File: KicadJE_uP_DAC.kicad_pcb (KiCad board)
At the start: 2 copper layers, 100 x 100 mm, 199 parts, among them J201 CV1, J202 CV2, J203 OUT1, J204 OUT2, J205 IN1, J206 IN2, J301 AVR-ISP-6, J302 UART, J401 CV1, J402 CV2, J403 OUT1, J404 OUT2, J405 OUT3, J406 OUT4, J407 IN1, J408 IN2, J409 I2C, J501 BOOT, J502 UART, J503 USB_B_Micro, P201 Doepfer_Power_16pin, P401 Doepfer_Power_16pin, SW201 SW_SPDT, SW401 SW_SPDT, U201 TL072, U202 MCP4822, U301 ATmega32A-AU, U401 TL072, U402 TL072, U405 MCP4822, U501 AMS1117-3.3, U502 STM32F103C8Tx, Y301 16MHz, Y501 8 MHz

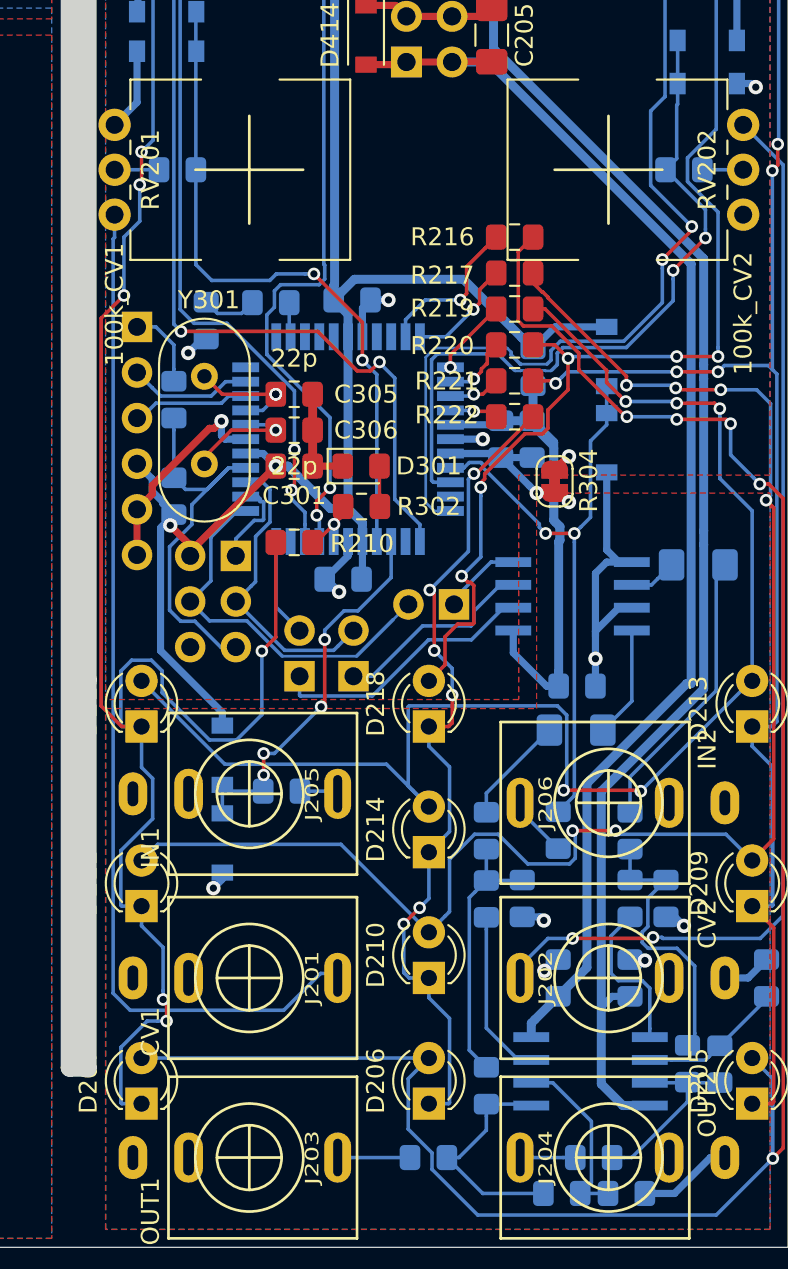
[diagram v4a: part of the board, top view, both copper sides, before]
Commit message: Silk update - DDS1 and DDS2 routed
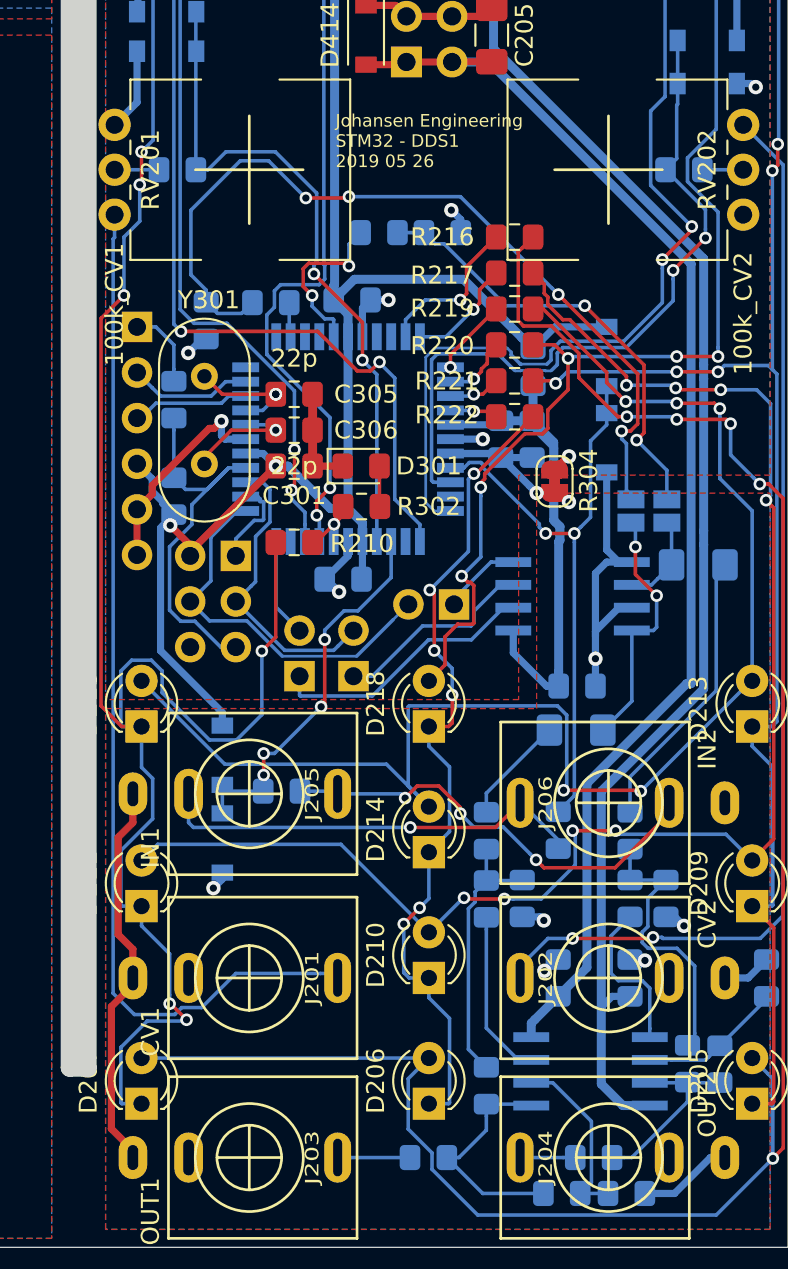
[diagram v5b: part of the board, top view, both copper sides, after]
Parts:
- added C213: 100n, Capacitor_SMD:C_0805_2012Metric_Pad1.15x1.40mm_HandSolder, B.Cu at (130.8, 93.5)
- added JP203: PWM1, Jumper:SolderJumper-2_P1.3mm_Open_Pad1.0x1.5mm, B.Cu at (141.2, 109.0)
- added JP205: PWM2, Jumper:SolderJumper-2_P1.3mm_Open_Pad1.0x1.5mm, B.Cu at (143.2, 109.0)
- added R223: 1k, Resistor_SMD:R_0805_2012Metric_Pad1.15x1.40mm_HandSolder, B.Cu at (127.2, 93.5)
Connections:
- net 0_LED renamed 32_0_LED
- U301 pad 16: (no net) -> 32_15_PWM
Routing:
- net PWM12: track 3.08 -> 47.8 mm, vias 0 -> 4
- net PWM15: track 0.00 -> 25.1 mm, vias 0 -> 2
- net Net-(J205-PadT): track 2.16 -> 24.9 mm, vias 0 -> 3
- net GNDA: track 124.8 -> 146.7 mm
- net Net-(J205-PadTN): track 3.43 -> 24.2 mm, vias 0 -> 1
- net 32_15_PWM: track 0.00 -> 9.63 mm, vias 0 -> 2
- net DACA: track 6.21 -> 14.1 mm, vias 0 -> 2
- net R1_19: track 86.7 -> 84.1 mm, vias 6 -> 8
- net DACB: track 2.67 -> 5.13 mm
- net C2_0: track 119.6 -> 121.2 mm
- net GND: track 179.6 -> 181.0 mm, vias 17 -> 18
- net +5V: track 273.5 -> 274.2 mm
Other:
- board text added: "DDS1"
- board text added: "Johansen Engineering STM32 - DDS1 2019 05 26"
- board text removed: "VCO3"

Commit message: 555 PCB
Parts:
- added C601: 1u, Capacitor_SMD:C_1206_3216Metric_Pad1.42x1.75mm_HandSolder, B.Cu at (70.0, 20.0)
- added C602: 100n, Capacitor_SMD:C_0805_2012Metric_Pad1.15x1.40mm_HandSolder, B.Cu at (62.0, 16.0)
- added C603: 100n, Capacitor_SMD:C_0805_2012Metric_Pad1.15x1.40mm_HandSolder, B.Cu at (79.0, 20.0)
- added C604: 1u, Capacitor_SMD:C_1206_3216Metric_Pad1.42x1.75mm_HandSolder, B.Cu at (70.0, 16.0)
- added C605: 100n, Capacitor_SMD:C_0805_2012Metric_Pad1.15x1.40mm_HandSolder, B.Cu at (87.9, 8.28)
- added C606: 1n, Capacitor_SMD:C_0805_2012Metric_Pad1.15x1.40mm_HandSolder, B.Cu at (84.1, 5.33)
- added C607: 22n, Capacitor_SMD:C_0805_2012Metric_Pad1.15x1.40mm_HandSolder, B.Cu at (80.0, 25.0)
- added C608: 10n, Capacitor_SMD:C_0805_2012Metric_Pad1.15x1.40mm_HandSolder, B.Cu at (75.0, 29.0)
- added C609: 220n, Capacitor_SMD:C_0805_2012Metric_Pad1.15x1.40mm_HandSolder, B.Cu at (102.2, 11.9)
- added C610: 1n, Capacitor_SMD:C_0805_2012Metric_Pad1.15x1.40mm_HandSolder, B.Cu at (83.2, 11.2)
- added C611: 1n, Capacitor_SMD:C_0805_2012Metric_Pad1.15x1.40mm_HandSolder, B.Cu at (89.1, 15.5)
- added D601: 1N1007, Diode_SMD:D_SOD-123, B.Cu at (63.0, 11.0)
- added D602: 1N1007, Diode_SMD:D_SOD-123, B.Cu at (63.0, 20.0)
- added D603: 1N1007, Diode_SMD:D_SOD-123, B.Cu at (120.5, 43.0)
- added D604: 1N1007, Diode_SMD:D_SOD-123, B.Cu at (94.0, 23.0)
- added D605: 1N1007, Diode_SMD:D_SOD-123, B.Cu at (100.9, 20.9)
- added D606: 1N1007, Diode_SMD:D_SOD-123, B.Cu at (94.7, 18.6)
- added D607: LED, LED_THT:LED_D3.0mm, F.Cu at (99.0, 137.0)
- added D609: LED, LED_THT:LED_D3.0mm, F.Cu at (99.0, 149.0)
- added J601: CV1, AJ-Dropbox-Kicad:PJ301SM, F.Cu at (95.0, 130.0)
- added J602: FM_lin, AJ-Dropbox-Kicad:PJ301SM, F.Cu at (95.0, 143.0)
- added J603: Sync, AJ-Dropbox-Kicad:PJ301SM, F.Cu at (95.0, 118.0)
- added J604: PWM, AJ-Dropbox-Kicad:PJ301SM, F.Cu at (95.0, 105.0)
- added J605: Ramp, AJ-Dropbox-Kicad:PJ301SM, F.Cu at (105.0, 118.0)
- added J606: Tri, AJ-Dropbox-Kicad:PJ301SM, F.Cu at (105.0, 144.5)
- added J608: 555_Pulse, AJ-Dropbox-Kicad:PJ301SM, F.Cu at (105.0, 130.0)
- added P601: Doepfer_Power_10pin, Connectors_IDC:IDC-Header_2x05_Pitch2.54mm_Straight, B.Cu at (105.5, 69.5)
- added R601: 10k, Resistor_SMD:R_0805_2012Metric_Pad1.15x1.40mm_HandSolder, B.Cu at (93.9, 15.5)
- added R602: 12k, Resistor_SMD:R_0805_2012Metric_Pad1.15x1.40mm_HandSolder, B.Cu at (85.0, 26.0)
- added R603: 47k, Resistor_SMD:R_0805_2012Metric_Pad1.15x1.40mm_HandSolder, B.Cu at (79.0, 16.0)
- added R604: 150k, Resistor_SMD:R_0805_2012Metric_Pad1.15x1.40mm_HandSolder, B.Cu at (114.1, 34.3)
- added R605: 100k, Resistor_SMD:R_0805_2012Metric_Pad1.15x1.40mm_HandSolder, B.Cu at (100.0, 17.8)
- added R606: 100r, Resistor_SMD:R_0805_2012Metric_Pad1.15x1.40mm_HandSolder, B.Cu at (75.0, 25.0)
- added R607: LDR03, OptoDevice:R_LDR_4.9x4.2mm_P2.54mm_Vertical, B.Cu at (79.0, 35.0)
- added R608: 1k5, Resistor_SMD:R_0805_2012Metric_Pad1.15x1.40mm_HandSolder, B.Cu at (87.0, 35.0)
- added R609: 100k, Resistor_SMD:R_0805_2012Metric_Pad1.15x1.40mm_HandSolder, B.Cu at (115.9, 25.5)
- added R610: 47k, Resistor_SMD:R_0805_2012Metric_Pad1.15x1.40mm_HandSolder, B.Cu at (90.0, 39.0)
- added R611: 10k, Resistor_SMD:R_0805_2012Metric_Pad1.15x1.40mm_HandSolder, B.Cu at (93.6, 3.67)
- added R612: 10k, Resistor_SMD:R_0805_2012Metric_Pad1.15x1.40mm_HandSolder, B.Cu at (102.2, 14.8)
- added R613: 10k, Resistor_SMD:R_0805_2012Metric_Pad1.15x1.40mm_HandSolder, B.Cu at (93.6, 6.62)
- added R614: 20k, Resistor_SMD:R_0805_2012Metric_Pad1.15x1.40mm_HandSolder, B.Cu at (120.6, 31.4)
- added R615: 1k, Resistor_SMD:R_0805_2012Metric_Pad1.15x1.40mm_HandSolder, B.Cu at (110.9, 21.1)
- added R616: 47k, Resistor_SMD:R_0805_2012Metric_Pad1.15x1.40mm_HandSolder, B.Cu at (120.4, 22.5)
- added R617: 47k, Resistor_SMD:R_0805_2012Metric_Pad1.15x1.40mm_HandSolder, B.Cu at (115.9, 28.4)
- added R618: 47k, Resistor_SMD:R_0805_2012Metric_Pad1.15x1.40mm_HandSolder, B.Cu at (104.7, 17.8)
- added R619: 47k, Resistor_SMD:R_0805_2012Metric_Pad1.15x1.40mm_HandSolder, B.Cu at (88.9, 2.38)
- added R620: 62k, Resistor_SMD:R_0805_2012Metric_Pad1.15x1.40mm_HandSolder, B.Cu at (115.9, 31.4)
- added R621: 100k_test, Resistor_SMD:R_0805_2012Metric_Pad1.15x1.40mm_HandSolder, B.Cu at (111.1, 25.9)
- added R622: 100k_test, Resistor_SMD:R_0805_2012Metric_Pad1.15x1.40mm_HandSolder, B.Cu at (88.9, 5.33)
- added R623: 62k, Resistor_SMD:R_0805_2012Metric_Pad1.15x1.40mm_HandSolder, B.Cu at (92.7, 9.57)
- added R624: 10k, Resistor_SMD:R_0805_2012Metric_Pad1.15x1.40mm_HandSolder, B.Cu at (82.0, 30.0)
- added R625: 1k, Resistor_SMD:R_0805_2012Metric_Pad1.15x1.40mm_HandSolder, B.Cu at (97.4, 9.57)
- added R626: 10k, Resistor_SMD:R_0805_2012Metric_Pad1.15x1.40mm_HandSolder, B.Cu at (111.1, 28.9)
- added R627: 20k, Resistor_SMD:R_0805_2012Metric_Pad1.15x1.40mm_HandSolder, B.Cu at (111.7, 15.2)
- added R628: 10k, Resistor_SMD:R_0805_2012Metric_Pad1.15x1.40mm_HandSolder, B.Cu at (103.1, 8.92)
- added R629: 2k, Resistor_SMD:R_0805_2012Metric_Pad1.15x1.40mm_HandSolder, B.Cu at (114.2, 18.2)
- added R630: 2k, Resistor_SMD:R_0805_2012Metric_Pad1.15x1.40mm_HandSolder, B.Cu at (120.6, 25.5)
- added R631: 2k2, Resistor_SMD:R_0805_2012Metric_Pad1.15x1.40mm_HandSolder, B.Cu at (106.9, 11.9)
- added R632: 2M2, Resistor_SMD:R_0805_2012Metric_Pad1.15x1.40mm_HandSolder, B.Cu at (98.4, 3.67)
- added R633: 3k, Resistor_SMD:R_0805_2012Metric_Pad1.15x1.40mm_HandSolder, B.Cu at (120.6, 28.4)
- added R634: 150k, Resistor_SMD:R_0805_2012Metric_Pad1.15x1.40mm_HandSolder, B.Cu at (93.6, 0.72)
- added R635: 100k, Resistor_SMD:R_0805_2012Metric_Pad1.15x1.40mm_HandSolder, B.Cu at (115.7, 22.5)
- added R636: 1k8, Resistor_SMD:R_0805_2012Metric_Pad1.15x1.40mm_HandSolder, B.Cu at (98.4, 6.62)
- added R637: 100k, Resistor_SMD:R_0805_2012Metric_Pad1.15x1.40mm_HandSolder, B.Cu at (106.9, 14.8)
- added RV601: 100k FM, Potentiometer_THT:Potentiometer_China_RK09_Single_Vertical_AJ, F.Cu at (92.5, 59.9)
- added RV603: 100k CV1, Potentiometer_THT:Potentiometer_China_RK09_Single_Vertical_AJ, F.Cu at (107.5, 87.5)
- added U601: TLC555, AJ-Dropbox-Kicad:AJ_SO-8_5.3x6.2mm_P1.27mm, B.Cu at (96.0, 68.0)
- added U602: TL074, Package_SO:SOIC-14_3.9x8.7mm_P1.27mm, F.Cu at (96.5, 75.0)
- added U603: TL074, Package_SO:SOIC-14_3.9x8.7mm_P1.27mm, B.Cu at (103.5, 105.0)
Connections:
- C202 pad 1: GNDA -> GND
- C203 pad 1: GNDA -> GND
- C204 pad 1: GNDA -> GND
- C208 pad 2: GNDA -> GND
- C211 pad 2: GNDA -> GND
- C304 pad 1: GNDA -> GND
- C402 pad 1: GNDA -> GND
- C403 pad 1: GNDA -> GND
- C409 pad 2: GNDA -> GND
- C410 pad 2: GNDA -> GND
- C415 pad 2: GNDA -> GND
- C416 pad 2: GNDA -> GND
- C506 pad 1: GNDA -> GND
- D212 pad 2: GNDA -> GND
- D220 pad 2: GNDA -> GND
- D420 pad 2: GNDA -> GND
- D422 pad 2: GNDA -> GND
- J201 pad S: GNDA -> GND
- J202 pad S: GNDA -> GND
- J203 pad S: GNDA -> GND
- J204 pad S: GNDA -> GND
- J205 pad S: GNDA -> GND
- J206 pad S: GNDA -> GND
- J401 pad S: GNDA -> GND
- J402 pad S: GNDA -> GND
- J403 pad S: GNDA -> GND
- J404 pad S: GNDA -> GND
- J405 pad S: GNDA -> GND
- J406 pad S: GNDA -> GND
- J407 pad S: GNDA -> GND
- J408 pad S: GNDA -> GND
- R206 pad 1: GNDA -> GND
- R212 pad 1: GNDA -> GND
- R303 pad 2: GNDA -> GND
- R304 pad 1: GNDA -> GND
- R403 pad 1: GNDA -> GND
- R405 pad 1: GNDA -> GND
- R413 pad 1: GNDA -> GND
- R415 pad 1: GNDA -> GND
- R418 pad 1: GNDA -> GND
- R426 pad 1: GNDA -> GND
- R505 pad 1: GNDA -> GND
- U202 pad 5: GNDA -> GND
- U202 pad 7: GNDA -> GND
- U301 pad 29: GNDA -> GND
- U405 pad 5: GNDA -> GND
- U405 pad 7: GNDA -> GND
- U502 pad 8: GNDA -> GND
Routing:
- net GNDA: track 146.7 -> 0.00 mm, vias 23 -> 0
- net GND: track 181.0 -> 327.7 mm, vias 18 -> 41
- added copper zone on B.Cu, net +12V
- removed copper zone on B.Cu, net +5VA
- removed copper zone on F.Cu, net GNDA

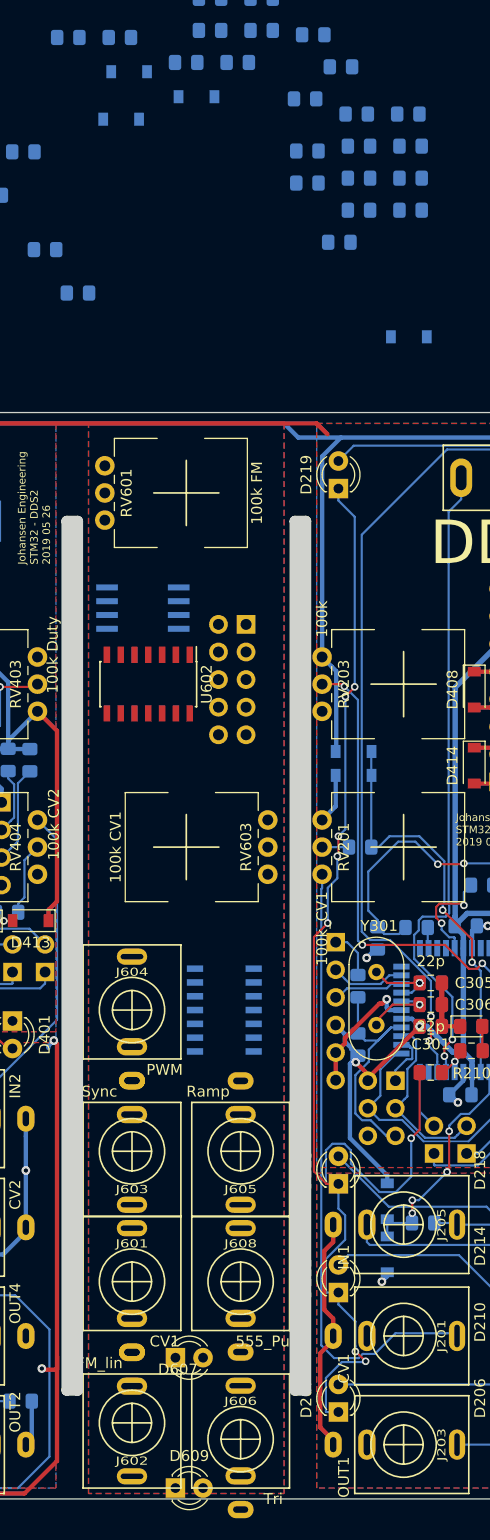
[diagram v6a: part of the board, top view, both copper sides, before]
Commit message: Placing outputs and Pots 555
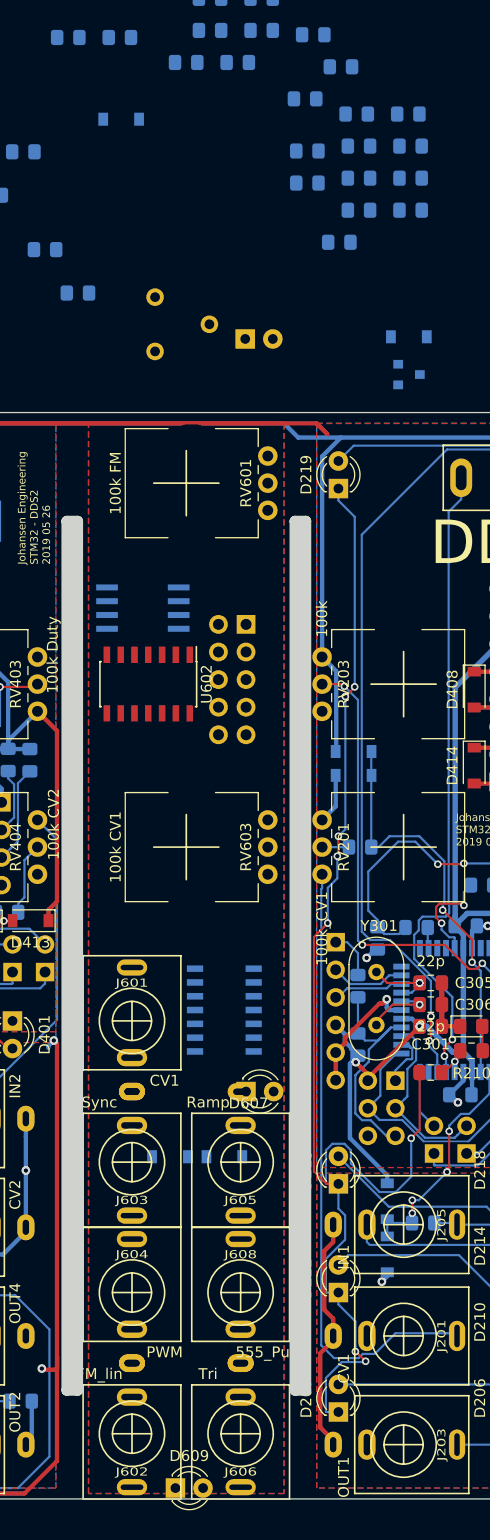
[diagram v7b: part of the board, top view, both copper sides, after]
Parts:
- added D611: Vactrol, LED_THT:LED_D3.0mm, B.Cu at (105.4, 43.2)
- added Q601: MMBT2222A, Package_TO_SOT_SMD:SOT-23, B.Cu at (120.5, 46.5)
- added RV602: 5k, Potentiometer_THT:Potentiometer_Piher_PT-6-V_Vertical, B.Cu at (97.1, 39.4)
- moved D606 100.3 mm to (103.5, 118.5)
- moved D605 97.6 mm to (98.5, 118.5)
- moved J604 26.0 mm to (95.0, 131.0)
- moved D607 25.3 mm to (105.5, 112.5)
- moved J601 24.0 mm to (95.0, 106.0)
- moved RV601 16.1 mm to (107.5, 54.0), turned to 180 degrees
- moved J602 1.00 mm to (95.0, 144.0)
- moved J603 1.00 mm to (95.0, 119.0)
- moved J605 1.00 mm to (105.0, 119.0)
- moved J608 1.00 mm to (105.0, 131.0)
- moved J606 0.50 mm to (105.0, 144.0), turned to 180 degrees
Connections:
- R625 pad 1: (no net) -> Net-(R625-Pad1)
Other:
- net class Default: trace_width 0.2 -> 0.15

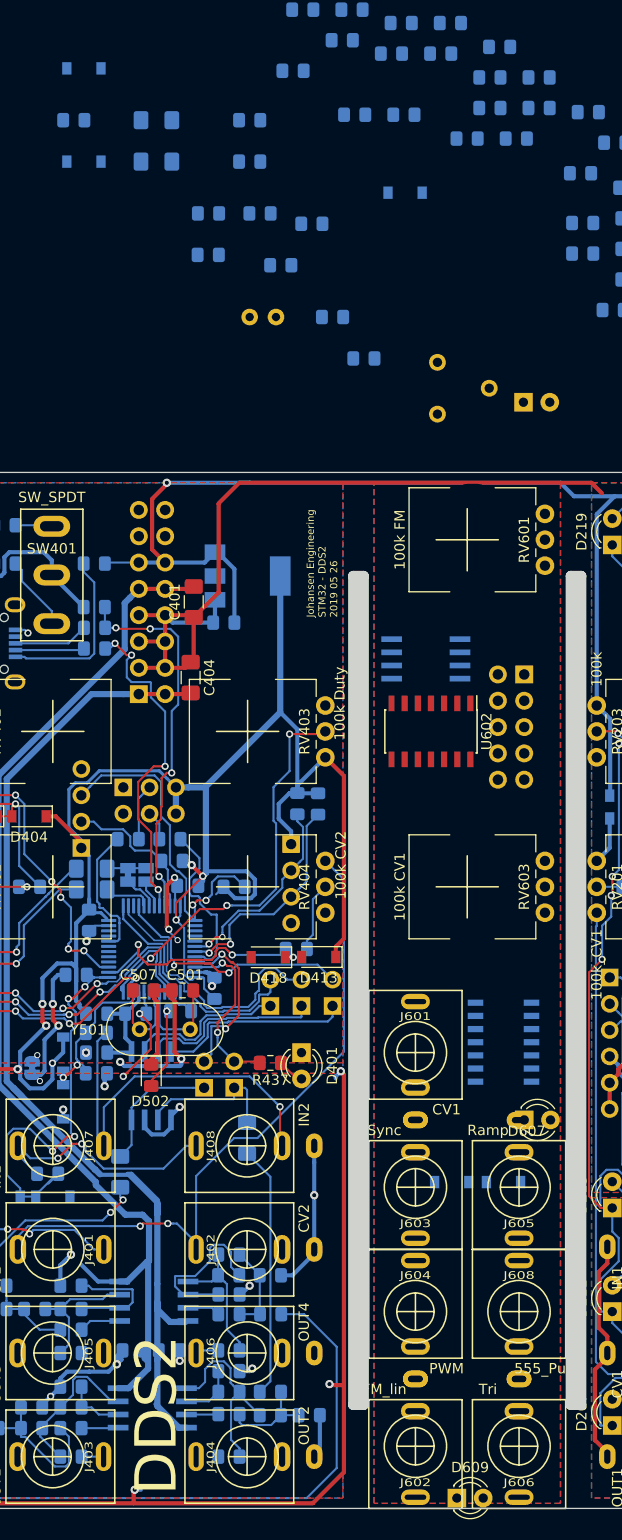
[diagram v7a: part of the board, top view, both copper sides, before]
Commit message: 555 Pwr to U603
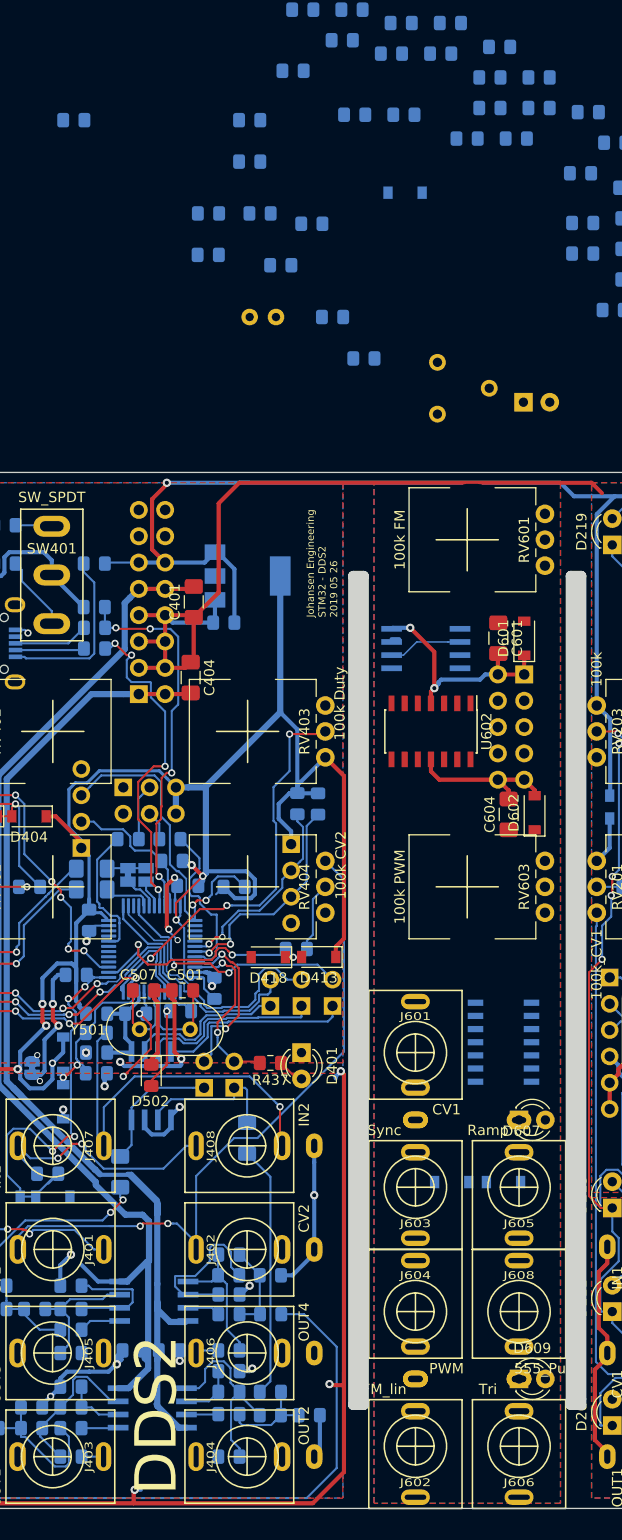
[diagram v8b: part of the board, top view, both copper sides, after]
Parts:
- C601, C604, D601, D602: moved to F.Cu
- RV603: value 100k CV1 -> 100k PWM
- moved D602 76.4 mm to (106.5, 82.8), turned to 90 degrees
- moved C604 75.1 mm to (104.0, 83.0), turned to 90 degrees
- moved D601 69.5 mm to (105.5, 66.0), turned to 90 degrees
- moved C601 56.6 mm to (103.0, 66.0), turned to 270 degrees
- moved D609 13.0 mm to (105.0, 137.5)
- moved U601 1.00 mm to (96.0, 67.0)
- moved D607 0.50 mm to (105.0, 112.5)
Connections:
- J601 pad S: Net-(J601-PadS) -> GND
- J601 pad TN: Net-(J601-PadS) -> GND
- J602 pad S: Net-(J601-PadS) -> GND
- J602 pad TN: Net-(J601-PadS) -> GND
- J603 pad S: Net-(J601-PadS) -> GND
- J603 pad TN: Net-(J601-PadS) -> GND
- J604 pad S: Net-(J601-PadS) -> GND
- J604 pad TN: Net-(J601-PadS) -> GND
- U603 pad 11: (no net) -> -12V
- U603 pad 4: (no net) -> +12V
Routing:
- net +12V: track 193.9 -> 218.1 mm, vias 0 -> 2
- net -12V: track 188.1 -> 203.3 mm
- net 555_In: track 0.00 -> 7.13 mm
- net 555_Dis: track 0.00 -> 0.72 mm
